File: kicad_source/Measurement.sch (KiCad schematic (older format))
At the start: 6 parts, among them P1 WR-TBL_691322310002

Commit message: generated pdf files
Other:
- note added: "Copyright generationmake 2019\nsee full project documentation at https://github.com/generationmake/StepperMotorFeatherWing"
- note removed: "Copyright generationmake 2019\nsee full project documentation at http://arduhmi.generationmake.de"
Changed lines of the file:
@@
 Sheet 2 6
 Title "HighPowerMotorFeatherWing"
-Date "2019-12-01"
+Date "2019-12-31"
 Rev "1.0"
 Comp "generationmake"
@@
 $EndDescr
 Text Notes 500  650  0    47   ~ 0
-Copyright generationmake 2019\nsee full project documentation at http://arduhmi.generationmake.de
+Copyright generationmake 2019\nsee full project documentation at https://github.com/generationmake/StepperMotorFeatherWing
 Text Notes 7000 6900 0    43   ~ 0
 You may redistribute and modify this documentation under the terms of the CERN OHL v.1.2. (http://ohwr.org/cernohl). \nThis documentation is distributed WITHOUT ANY EXPRESS OR IMPLIED WARRANTY, INCLUDING OF MERCHANTABILITY, SATISFACTORY \nQUALITY AND FITNESS FOR A PARTICULAR PURPOSE. Please see the CERN OHL v.1.2  for applicable conditions

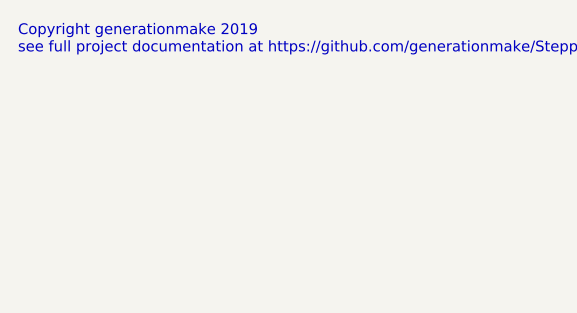
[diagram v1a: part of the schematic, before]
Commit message: added leds and decoupling capacitors
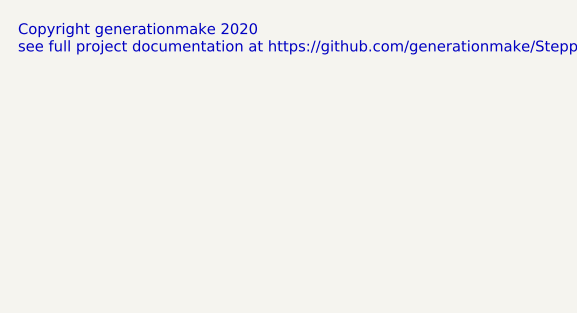
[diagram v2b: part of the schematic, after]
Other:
- note added: "Copyright generationmake 2020\nsee full project documentation at https://github.com/generationmake/StepperMotorFeatherWing"
- note removed: "Copyright generationmake 2019\nsee full project documentation at https://github.com/generationmake/StepperMotorFeatherWing"
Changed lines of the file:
@@
 Sheet 2 6
 Title "HighPowerMotorFeatherWing"
-Date "2019-12-31"
-Rev "1.0"
+Date "2020-07-04"
+Rev "1.1"
 Comp "generationmake"
 Comment1 ""
@@
 $EndDescr
 Text Notes 500  650  0    47   ~ 0
-Copyright generationmake 2019\nsee full project documentation at https://github.com/generationmake/StepperMotorFeatherWing
+Copyright generationmake 2020\nsee full project documentation at https://github.com/generationmake/StepperMotorFeatherWing
 Text Notes 7000 6900 0    43   ~ 0
 You may redistribute and modify this documentation under the terms of the CERN OHL v.1.2. (http://ohwr.org/cernohl). \nThis documentation is distributed WITHOUT ANY EXPRESS OR IMPLIED WARRANTY, INCLUDING OF MERCHANTABILITY, SATISFACTORY \nQUALITY AND FITNESS FOR A PARTICULAR PURPOSE. Please see the CERN OHL v.1.2  for applicable conditions

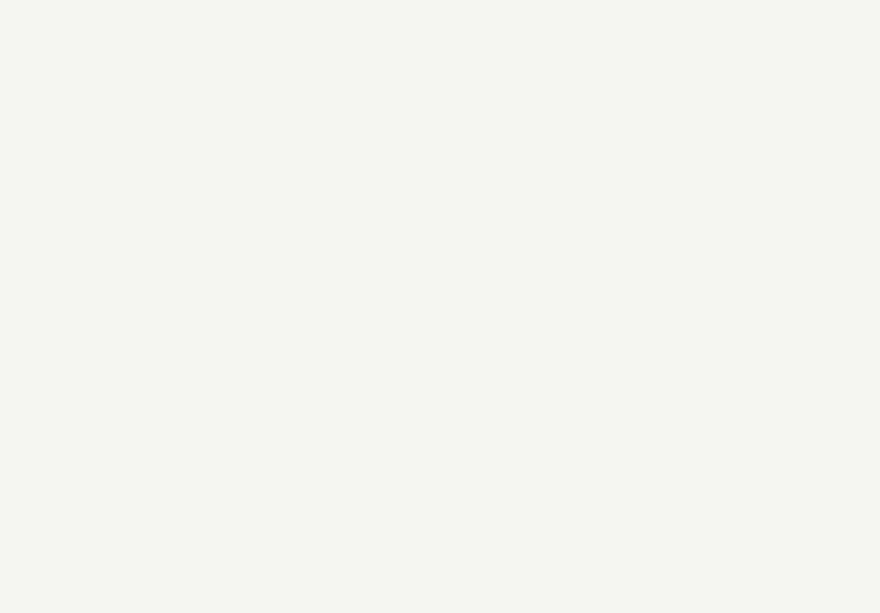
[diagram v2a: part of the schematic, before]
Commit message: added temperature sensor LM75
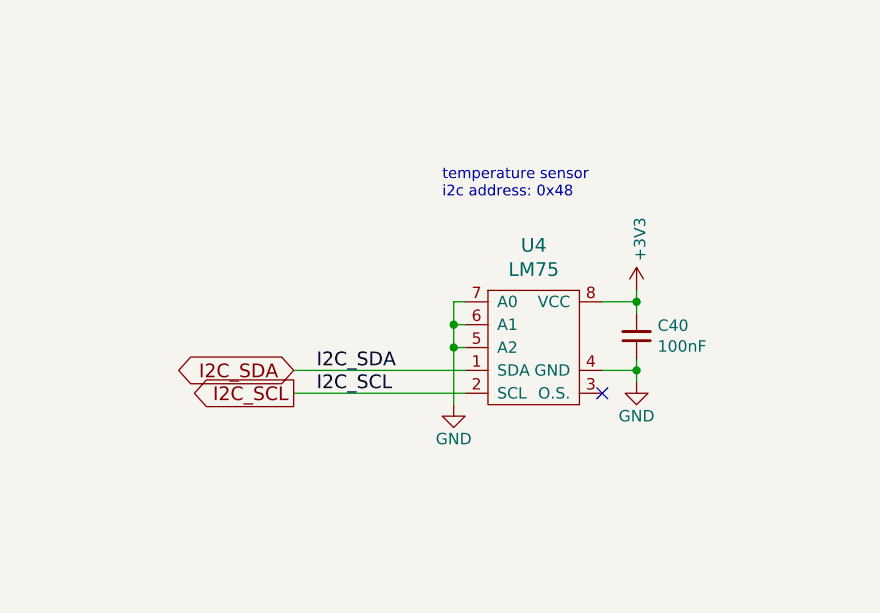
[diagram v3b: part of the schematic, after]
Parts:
- added C40: 100nF, capacitors:C_0603, symbol devices:C_0603
- added U4: LM75, SOIC:SOIC-8_3.9x4.9mm_Pitch1.27mm, symbol IC_sensor:LM75
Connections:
- net +3V3: now also C40.2, U4.8 (VCC)
- net GND: now also C40.1, U4.4 (GND), U4.5 (A2), U4.6 (A1), U4.7 (A0)
- new net I2C_SCL: U4.2 (SCL)
- new net I2C_SDA: U4.1 (SDA)
- no-connect marks 0 -> 1
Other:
- note added: "temperature sensor\ni2c address: 0x48"
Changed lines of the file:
@@
 	4950 4800 4850 4800
 Connection ~ 4850 4800
+$Comp
+L IC_sensor:LM75 U?
+U 1 1 5F020063
+P 7150 3450
+AR Path="/5F020063" Ref="U?"  Part="1"
+AR Path="/5DE3661B/5F020063" Ref="U4"  Part="1"
+F 0 "U4" H 7150 3897 60  0000 C CNN
+F 1 "LM75" H 7150 3791 60  0000 C CNN
+F 2 "SOIC:SOIC-8_3.9x4.9mm_Pitch1.27mm" H 7150 3450 60  0001 C CNN
+F 3 "" H 7150 3450 60  0001 C CNN
+	1    7150 3450
+	1    0    0    -1
+$EndComp
+$Comp
+L devices:C_0603 C?
+U 1 1 5F020069
+P 7600 3400
+AR Path="/5F020069" Ref="C?"  Part="1"
+AR Path="/5DE3661B/5F020069" Ref="C40"  Part="1"
+F 0 "C40" H 7508 3354 50  0000 R CNN
+F 1 "100nF" H 7508 3445 50  0000 R CNN
+F 2 "capacitors:C_0603" H 7600 3250 50  0001 C CNN
+F 3 "" H 7600 3400 50  0000 C CNN
+	1    7600 3400
+	-1   0    0    1
+$EndComp
+$Comp
+L StepperMotorFeatherWing-rescue:+3V3-power-supply-MKRHMIShield-rescue-MKRHMIShield-rescue-HMIFeatherWing-rescue-HighPowerMotorFeatherWing-rescue #PWR?
+U 1 1 5F02006F
+P 7600 3200
+AR Path="/5F02006F" Ref="#PWR?"  Part="1"
+AR Path="/5DE3661B/5F02006F" Ref="#PWR?"  Part="1"
+F 0 "#PWR?" H 7600 3050 50  0001 C CNN
+F 1 "+3V3" V 7615 3328 50  0000 L CNN
+F 2 "" H 7600 3200 50  0000 C CNN
+F 3 "" H 7600 3200 50  0000 C CNN
+	1    7600 3200
+	1    0    0    -1
+$EndComp
+$Comp
+L StepperMotorFeatherWing-rescue:GND-ArduHMIShield-rescue-ArduHMIShield-rescue-MKRHMIShield-rescue-MKRHMIShield-rescue-HMIFeatherWing-rescue-HighPowerMotorFeatherWing-rescue #PWR?
+U 1 1 5F020075
+P 7600 3600
+AR Path="/5F020075" Ref="#PWR?"  Part="1"
+AR Path="/5DE3661B/5F020075" Ref="#PWR?"  Part="1"
+F 0 "#PWR?" H 7600 3350 50  0001 C CNN
+F 1 "GND" H 7600 3450 50  0000 C CNN
+F 2 "" H 7600 3600 50  0000 C CNN
+F 3 "" H 7600 3600 50  0000 C CNN
+	1    7600 3600
+	1    0    0    -1
+$EndComp
+NoConn ~ 7450 3650
+$Comp
+L StepperMotorFeatherWing-rescue:GND-ArduHMIShield-rescue-ArduHMIShield-rescue-MKRHMIShield-rescue-MKRHMIShield-rescue-HMIFeatherWing-rescue-HighPowerMotorFeatherWing-rescue #PWR?
+U 1 1 5F02007C
+P 6800 3700
+AR Path="/5F02007C" Ref="#PWR?"  Part="1"
+AR Path="/5DE3661B/5F02007C" Ref="#PWR?"  Part="1"
+F 0 "#PWR?" H 6800 3450 50  0001 C CNN
+F 1 "GND" H 6800 3550 50  0000 C CNN
+F 2 "" H 6800 3700 50  0000 C CNN
+F 3 "" H 6800 3700 50  0000 C CNN
+	1    6800 3700
+	1    0    0    -1
+$EndComp
+Wire Wire Line
+	6100 3550 6850 3550
+Wire Wire Line
+	6100 3650 6850 3650
+Text Label 6200 3550 0    60   ~ 0
+I2C_SDA
+Text Label 6200 3650 0    60   ~ 0
+I2C_SCL
+Wire Wire Line
+	6850 3250 6800 3250
+Wire Wire Line
+	6800 3250 6800 3350
+Wire Wire Line
+	6850 3450 6800 3450
+Connection ~ 6800 3450
+Wire Wire Line
+	6800 3450 6800 3700
+Wire Wire Line
+	6850 3350 6800 3350
+Connection ~ 6800 3350
+Wire Wire Line
+	6800 3350 6800 3450
+Wire Wire Line
+	7600 3500 7600 3550
+Wire Wire Line
+	7600 3300 7600 3250
+Wire Wire Line
+	7450 3250 7600 3250
+Connection ~ 7600 3250
+Wire Wire Line
+	7600 3250 7600 3200
+Wire Wire Line
+	7450 3550 7600 3550
+Connection ~ 7600 3550
+Wire Wire Line
+	7600 3550 7600 3600
+Text Notes 6750 2800 0    47   ~ 0
+temperature sensor\ni2c address: 0x48
+Text GLabel 6100 3550 0    60   BiDi ~ 0
+I2C_SDA
+Text GLabel 6100 3650 0    60   Output ~ 0
+I2C_SCL
 $EndSCHEMATC

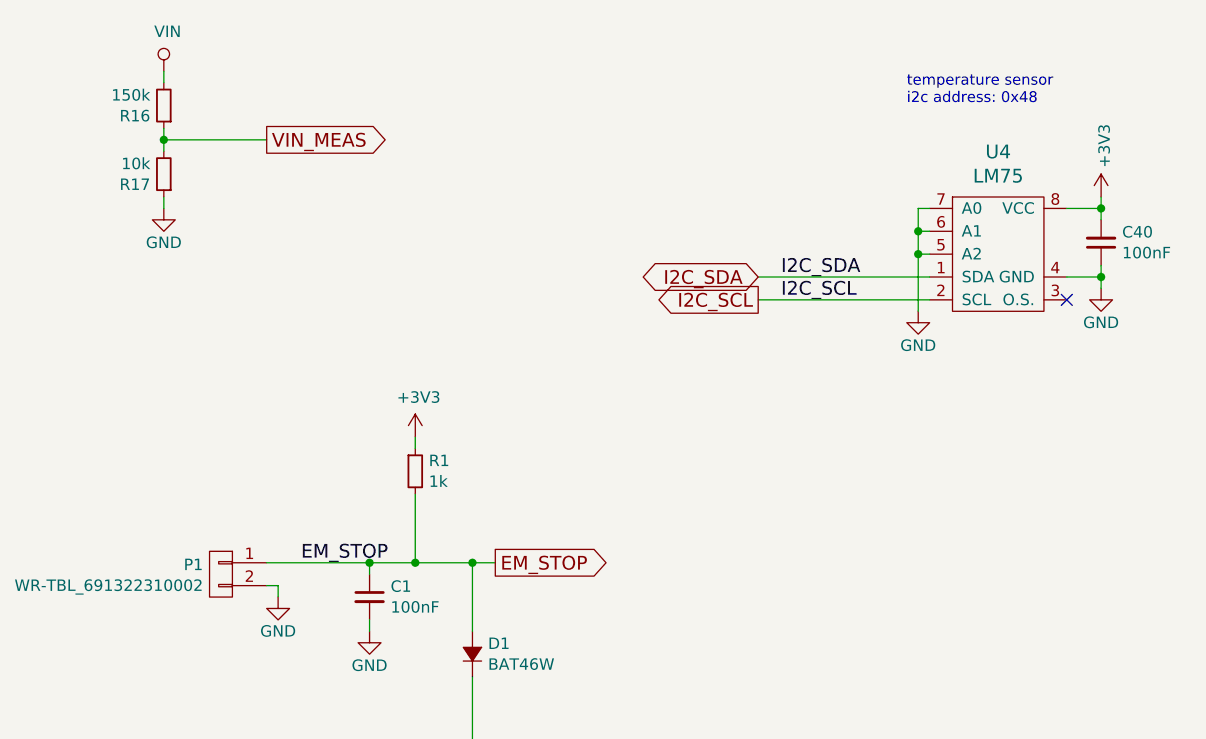
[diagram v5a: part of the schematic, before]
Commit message: updated part numbers
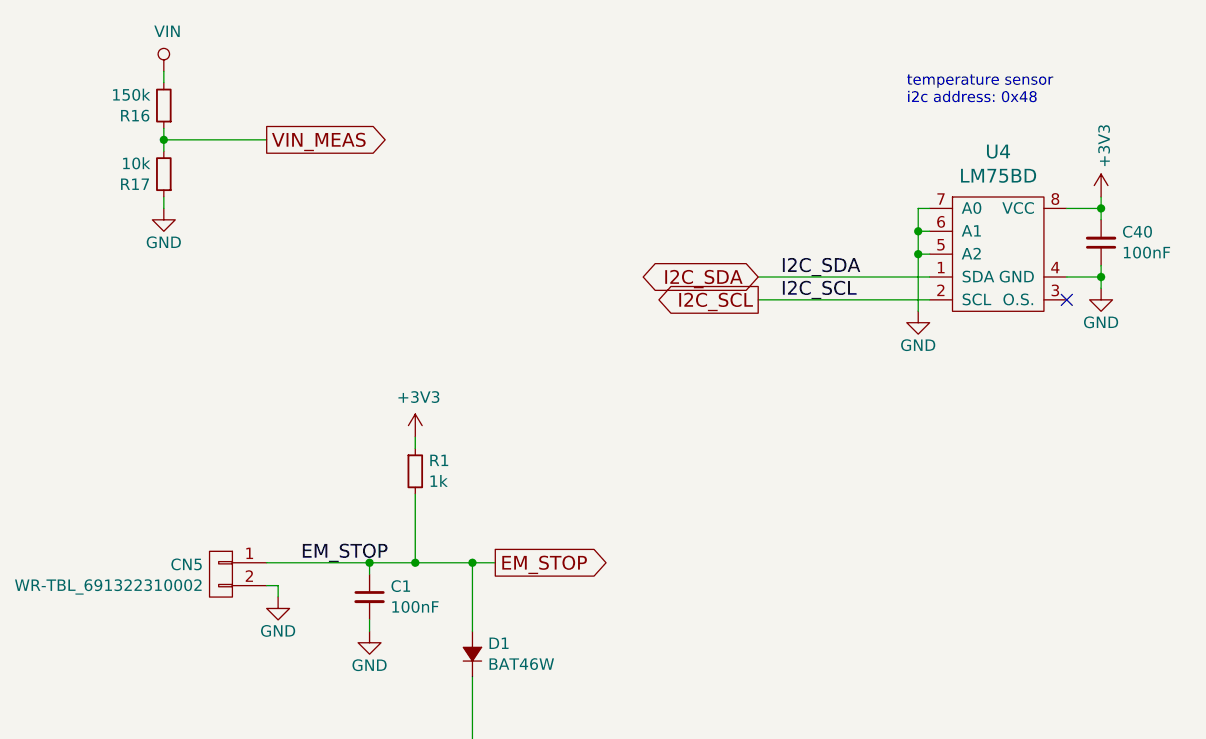
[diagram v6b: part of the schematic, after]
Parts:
- U4: value LM75 -> LM75BD
- renumbered P1 to CN5
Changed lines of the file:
@@
 P 3750 4850
 AR Path="/5DE3616E/5DFB2102" Ref="P?"  Part="1"
-AR Path="/5DE3661B/5DFB2102" Ref="P1"  Part="1"
-F 0 "P1" H 3828 4891 50  0000 L CNN
+AR Path="/5DE3661B/5DFB2102" Ref="CN5"  Part="1"
+F 0 "CN5" H 3828 4891 50  0000 L CNN
 F 1 "WR-TBL_691322310002" H 3828 4800 50  0000 L CNN
 F 2 "CON_wuerth:WR-TBL_691322310002" H 3650 4900 50  0001 C CNN
@@
 AR Path="/5DE3661B/5F020063" Ref="U4"  Part="1"
 F 0 "U4" H 7150 3897 60  0000 C CNN
-F 1 "LM75" H 7150 3791 60  0000 C CNN
+F 1 "LM75BD" H 7150 3791 60  0000 C CNN
 F 2 "SOIC:SOIC-8_3.9x4.9mm_Pitch1.27mm" H 7150 3450 60  0001 C CNN
 F 3 "" H 7150 3450 60  0001 C CNN

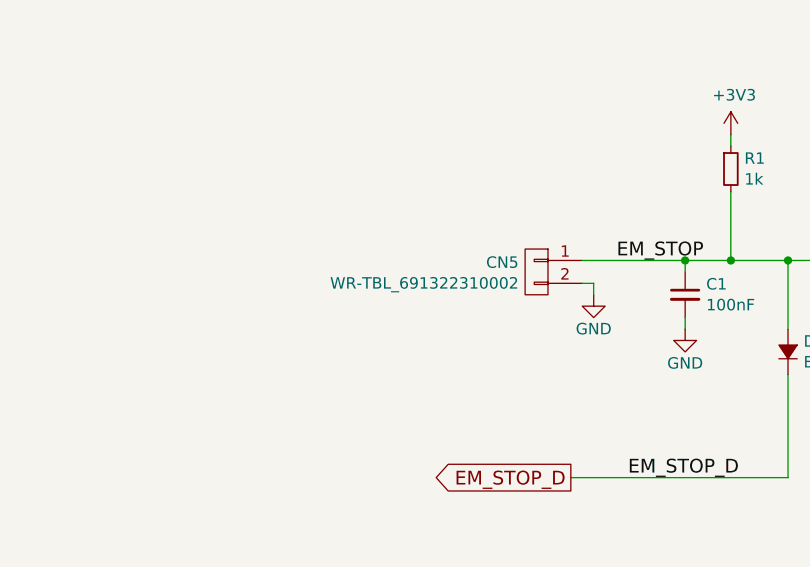
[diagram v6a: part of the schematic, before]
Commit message: updated part numbers
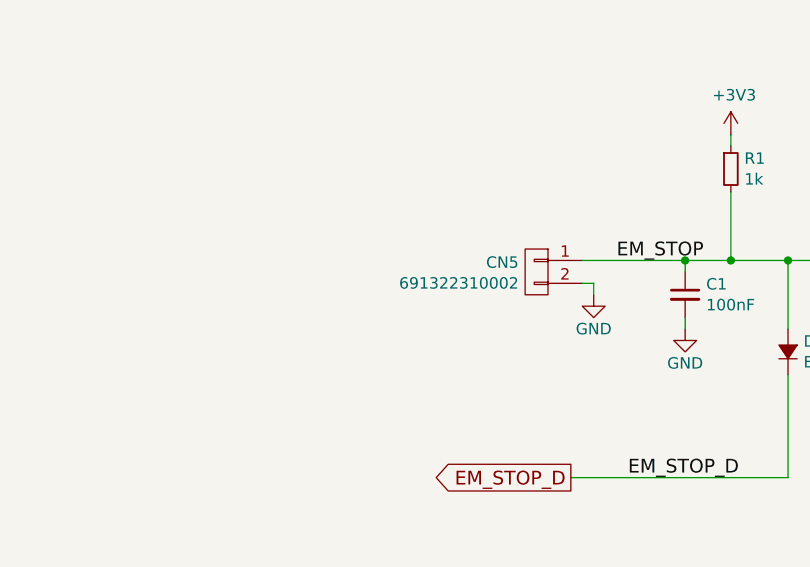
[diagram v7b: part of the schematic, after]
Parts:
- CN5: value WR-TBL_691322310002 -> 691322310002
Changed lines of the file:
@@
 AR Path="/5DE3661B/5DFB2102" Ref="CN5"  Part="1"
 F 0 "CN5" H 3828 4891 50  0000 L CNN
-F 1 "WR-TBL_691322310002" H 3828 4800 50  0000 L CNN
+F 1 "691322310002" H 3828 4800 50  0000 L CNN
 F 2 "CON_wuerth:WR-TBL_691322310002" H 3650 4900 50  0001 C CNN
 F 3 "" H 3750 4850 50  0000 C CNN
